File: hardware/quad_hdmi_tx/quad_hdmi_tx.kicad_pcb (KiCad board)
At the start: 4 copper layers, 115 x 110 mm, 147 parts, among them J1 HDMI_A, J2 HDMI_A, J3 HDMI_A, J4 HDMI_A, J5 USB-C 5V in, J6 5V ALT IN, J7 FPGA_J7, J8 FPGA_J8, U11 ADV7513BSWZ, U12 TPD12S016PWR, U13 TLV1117LV18DCYR, U21 ADV7513BSWZ, U22 TPD12S016PWR, U23 TLV1117LV18DCYR, U31 ADV7513BSWZ, U32 TPD12S016PWR, U33 TLV1117LV18DCYR, U41 ADV7513BSWZ, U42 TPD12S016PWR, U43 TLV1117LV18DCYR, U5 AP63203WU

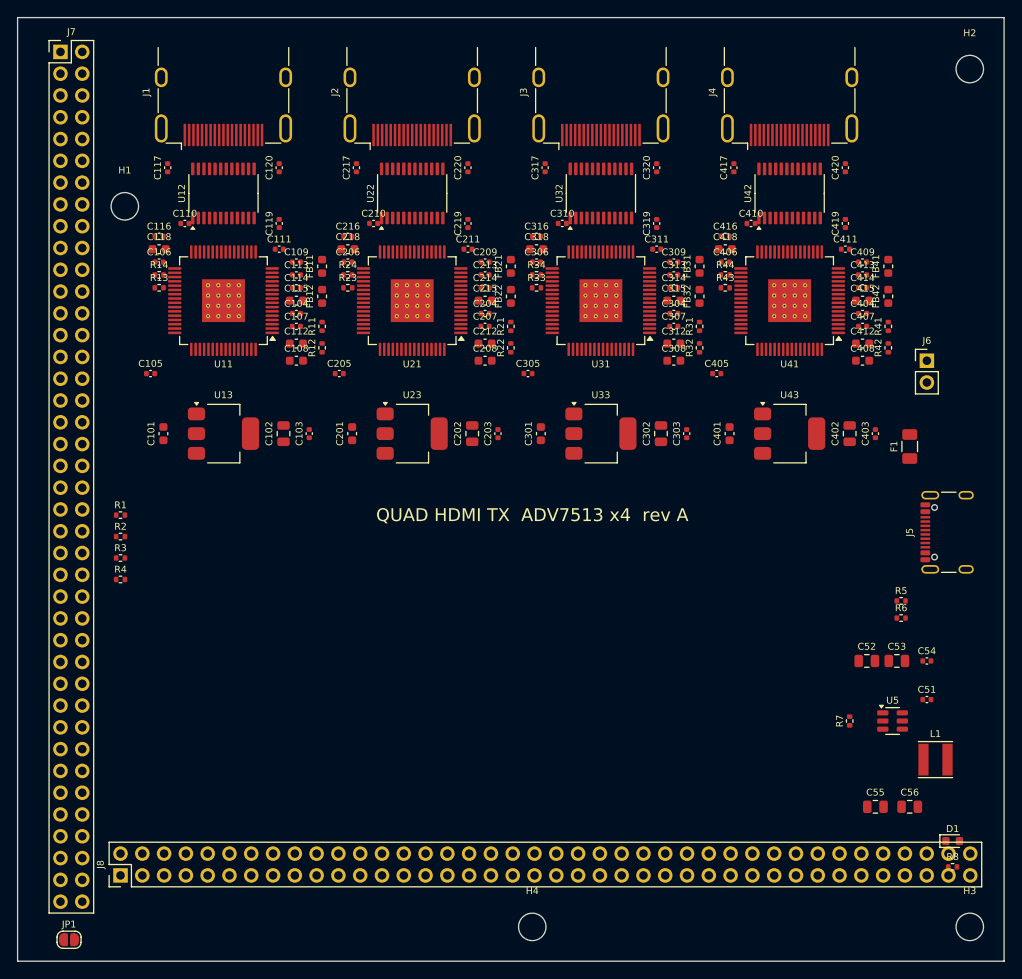
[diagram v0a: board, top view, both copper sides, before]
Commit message: レイアウト: プレーン系ネットのファンアウトビア生成、SES 取り込みの修正、チャネルピッチ 24 mm に変更
- FreeRouting は内層プレーンへのビアを作らないため、GND/+3V3/1V8 の全 SMD パッドに衝突チェック付きでビアを先置き
- 自前の SES パーサ (ses_import.py) を用意し、pcbnew API の取り込みが失敗した場合に使用
- FreeRouting の設定ファイル/GUI 要件などの注意点を README に記載

Co-Authored-By: Claude Fable 5.1 <noreply@anthropic.com>
Claude-Session: https://claude.ai/code/session_01JGo25NCpKCcdkj7JC5mDdQ
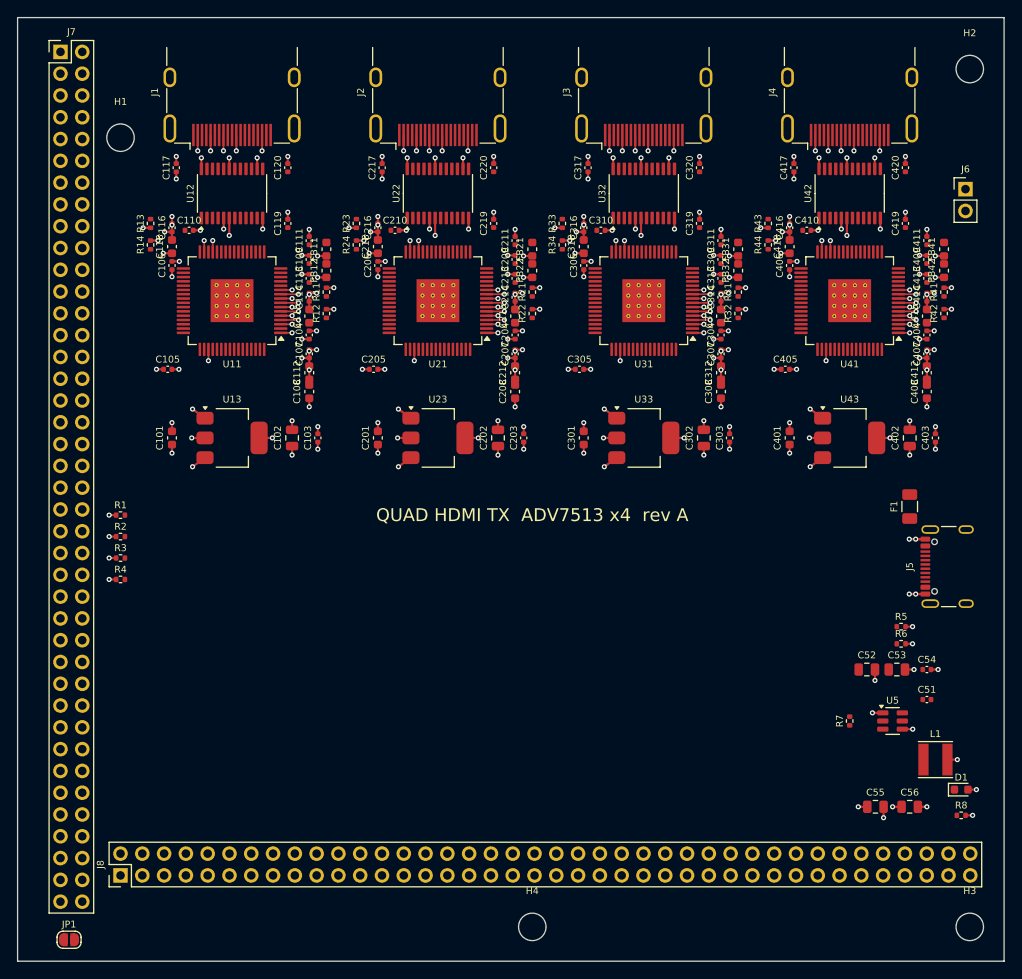
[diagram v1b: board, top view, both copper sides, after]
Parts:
- moved J6 20.5 mm to (110.5, 20.0)
- moved C411 9.55 mm to (106.0, 26.0), turned to 90 degrees
- moved R43 9.01 mm to (87.5, 24.0), turned to 90 degrees
- moved C408 8.32 mm to (106.0, 43.6), turned to 90 degrees
- moved C412 8.23 mm to (106.0, 41.4), turned to 90 degrees
- moved C407 8.15 mm to (106.0, 39.2), turned to 90 degrees
- moved R33 8.08 mm to (63.5, 24.0), turned to 90 degrees
- moved C405 8.02 mm to (89.5, 41.0)
- moved H1 8.02 mm to (12.0, 14.0)
- moved C404 7.91 mm to (106.0, 37.0), turned to 90 degrees
- moved C415 7.71 mm to (106.0, 34.8), turned to 90 degrees
- moved R41 7.63 mm to (108.0, 32.0)
- moved R42 7.63 mm to (108.0, 34.5)
- moved C414 7.58 mm to (106.0, 32.6), turned to 90 degrees
- moved C311 7.57 mm to (82.0, 26.0), turned to 90 degrees
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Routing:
- net GND: track 0.00 -> 224.3 mm, vias 0 -> 171
- net +3V3: track 0.00 -> 56.8 mm, vias 0 -> 51
- net CH4_1V8: track 0.00 -> 16.7 mm, vias 0 -> 15
- net CH1_1V8: track 0.00 -> 16.7 mm, vias 0 -> 15
- net CH3_1V8: track 0.00 -> 16.7 mm, vias 0 -> 15
- net CH2_1V8: track 0.00 -> 16.7 mm, vias 0 -> 15

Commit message: レイアウト: TMDS ペアを事前配線、ファンアウトの衝突チェック強化、配置とルールの修正
- TMDS 8 本/ch を ADV → TPD 下の U ターン → TPD パッド → コネクタ へ交差なしで固定配線
- ファンアウトビアは既存配線とも衝突チェック、内向き候補を追加、置けない GND ピンは隣接ピンへ短絡
- 1V8 の島を LDO 入力側と TPD 3.3V ビアを避ける多角形に変更、DVDD_3V ピン用スロット
- 最小ドリル 0.2 mm (ADV の EP サーマルビア)、コンデンサ列の間隔調整、シルクの参照記号を Fab 層へ
- 事前配線状態の DRC: クリアランス/コートヤード違反なし

Co-Authored-By: Claude Fable 5.1 <noreply@anthropic.com>
Claude-Session: https://claude.ai/code/session_01JGo25NCpKCcdkj7JC5mDdQ
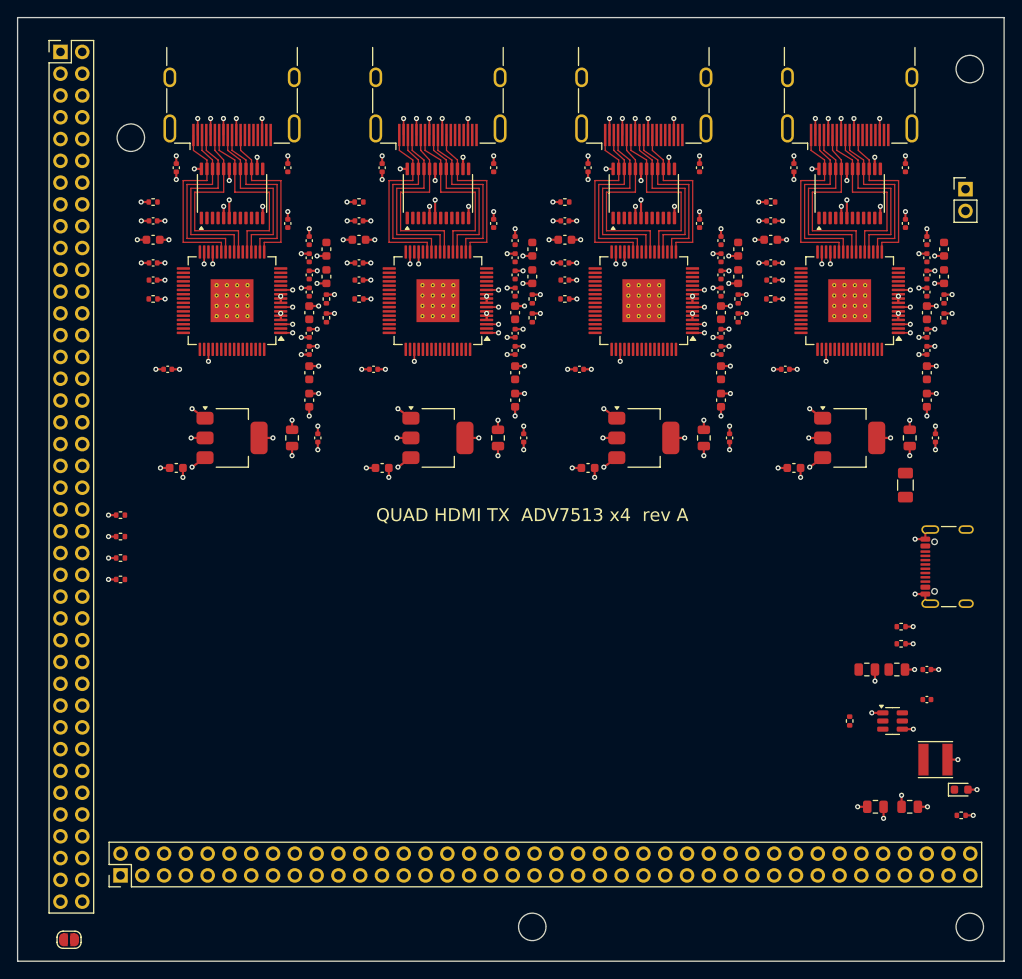
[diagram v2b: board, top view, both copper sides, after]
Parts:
- moved C210 7.16 mm to (39.8, 30.6)
- moved C310 7.16 mm to (63.8, 30.6)
- moved C410 7.16 mm to (87.8, 30.6)
- moved C110 7.16 mm to (15.8, 30.6)
- moved R14 6.31 mm to (15.8, 32.8), turned to 0 degrees
- moved R24 6.31 mm to (39.8, 32.8), turned to 0 degrees
- moved R34 6.31 mm to (63.8, 32.8), turned to 0 degrees
- moved R44 6.31 mm to (87.8, 32.8), turned to 0 degrees
- moved C101 3.54 mm to (18.5, 52.5), turned to 0 degrees
- moved C201 3.54 mm to (42.5, 52.5), turned to 0 degrees
- moved C301 3.54 mm to (66.5, 52.5), turned to 0 degrees
- moved C401 3.54 mm to (90.5, 52.5), turned to 0 degrees
- moved F1 2.55 mm to (103.5, 54.5)
- moved R13 2.52 mm to (15.8, 21.5), turned to 0 degrees
- moved R23 2.52 mm to (39.8, 21.5), turned to 0 degrees
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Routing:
- net GND: track 224.3 -> 191.0 mm, vias 171 -> 155
- net CH1_TX1_P: track 0.00 -> 22.5 mm
- net CH4_TX1_P: track 0.00 -> 22.5 mm
- net CH2_TX1_P: track 0.00 -> 22.5 mm
- net CH3_TX1_P: track 0.00 -> 22.5 mm
- net CH2_TX1_N: track 0.00 -> 22.5 mm
- net CH1_TX1_N: track 0.00 -> 22.5 mm
- net CH4_TX1_N: track 0.00 -> 22.5 mm
- net CH3_TX1_N: track 0.00 -> 22.5 mm
- net CH4_TX2_P: track 0.00 -> 21.7 mm
- net CH3_TX2_P: track 0.00 -> 21.7 mm
- net CH2_TX2_P: track 0.00 -> 21.7 mm
- net CH1_TX2_P: track 0.00 -> 21.7 mm
- net CH2_TX2_N: track 0.00 -> 21.7 mm
- net CH1_TX2_N: track 0.00 -> 21.7 mm
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
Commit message: レイアウト: 囲われたパッドへのアクセスビア、連続 GND ピンの数珠つなぎ、5V_OUT 事前配線、事前配線 DRC クリーン
Co-Authored-By: Claude Fable 5.1 <noreply@anthropic.com>
Claude-Session: https://claude.ai/code/session_01JGo25NCpKCcdkj7JC5mDdQ
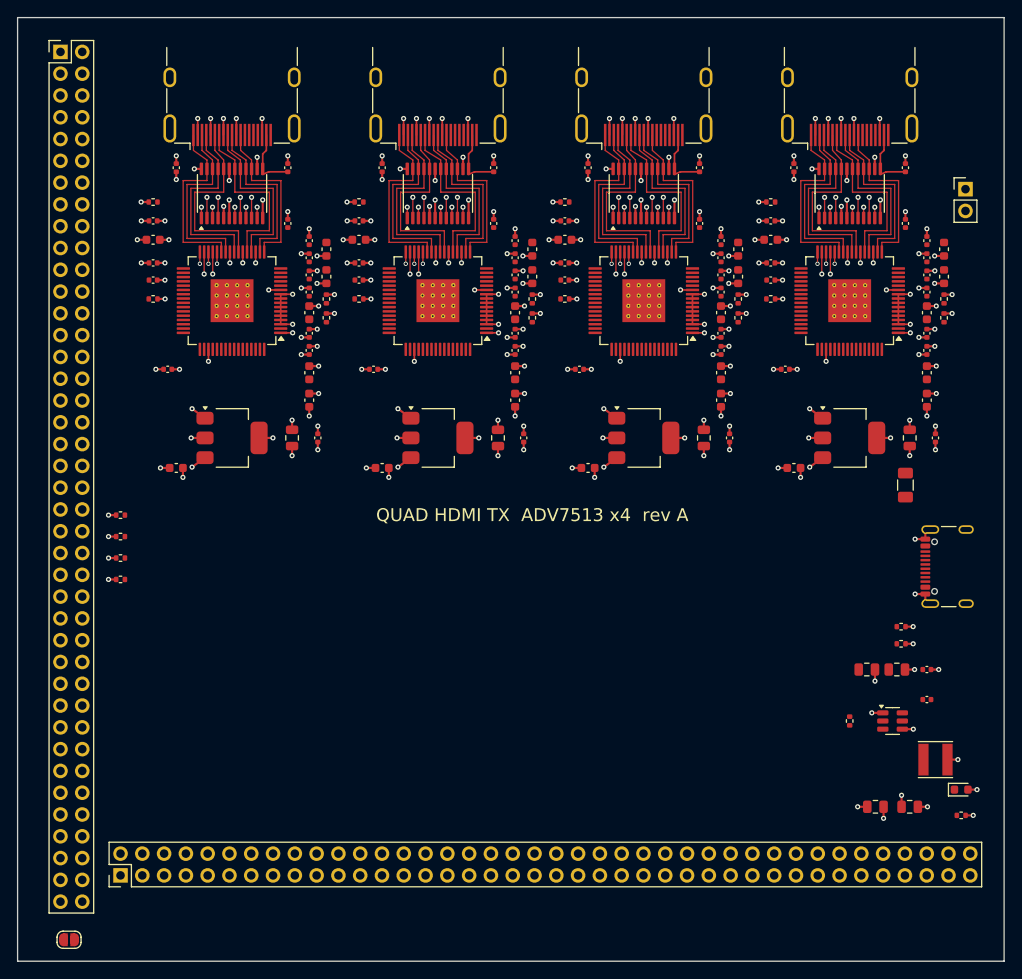
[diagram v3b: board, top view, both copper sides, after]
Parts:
- removed H1, H2, H3, H4: M3, MountingHole_3.2mm_M3
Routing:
- net +3V3: track 58.0 -> 65.7 mm
- net CH1_5V_OUT: track 0.00 -> 7.12 mm
- net CH4_5V_OUT: track 0.00 -> 7.12 mm
- net CH3_5V_OUT: track 0.00 -> 7.12 mm
- net CH2_5V_OUT: track 0.00 -> 7.12 mm
- net +5V: track 0.00 -> 5.05 mm, vias 0 -> 4
- net CH4_CEC_A: track 0.00 -> 2.64 mm, vias 0 -> 2
- net CH3_CEC_A: track 0.00 -> 2.64 mm, vias 0 -> 2
- net CH2_CEC_A: track 0.00 -> 2.64 mm, vias 0 -> 2
- net CH1_CEC_A: track 0.00 -> 2.64 mm, vias 0 -> 2
- net CH4_AVDD: track 0.00 -> 2.55 mm, vias 0 -> 2
- net CH3_AVDD: track 0.00 -> 2.55 mm, vias 0 -> 2
- net CH2_AVDD: track 0.00 -> 2.55 mm, vias 0 -> 2
- net CH1_AVDD: track 0.00 -> 2.55 mm, vias 0 -> 2
- net CH4_HPD_CONN: track 0.00 -> 2.41 mm, vias 0 -> 1
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
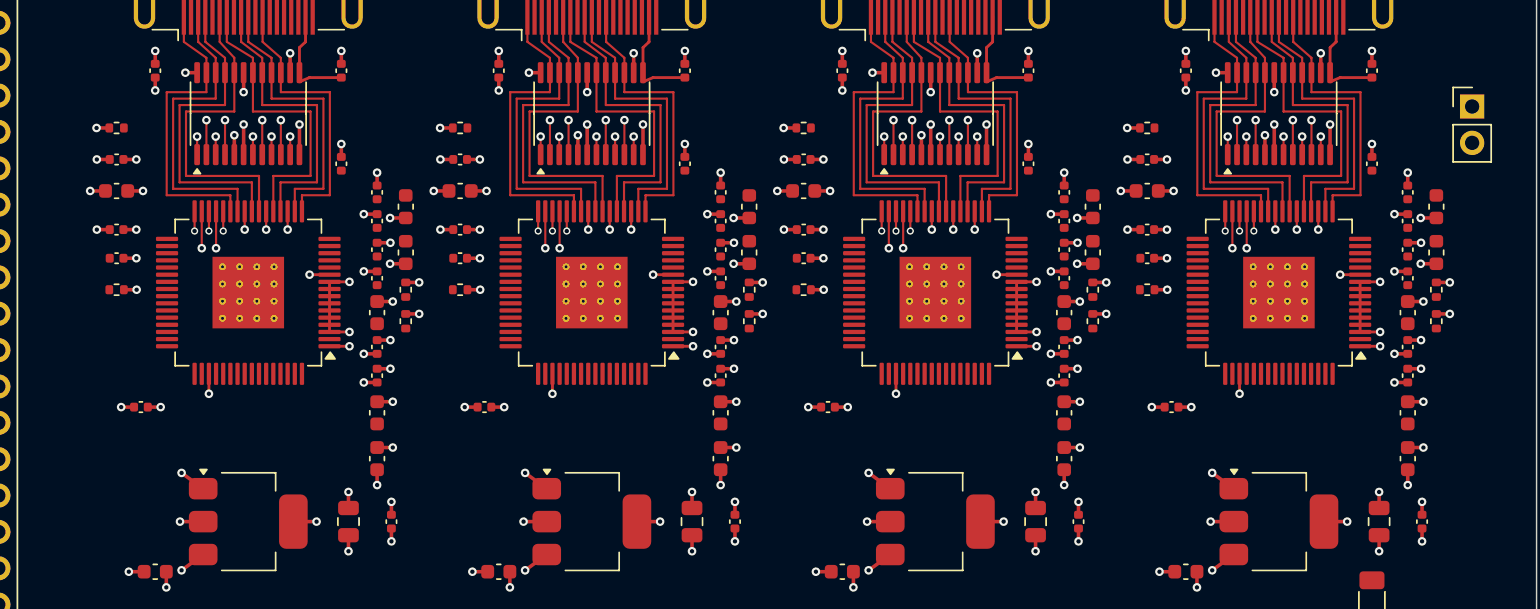
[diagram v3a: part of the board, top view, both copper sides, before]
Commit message: レイアウト: 左列を ADV 左上へ移動、1V8 の島を縮小、TPD 制御ピンと DVDD_3V の +3V3 事前配線、ビア掃除の修正
Co-Authored-By: Claude Fable 5.1 <noreply@anthropic.com>
Claude-Session: https://claude.ai/code/session_01JGo25NCpKCcdkj7JC5mDdQ
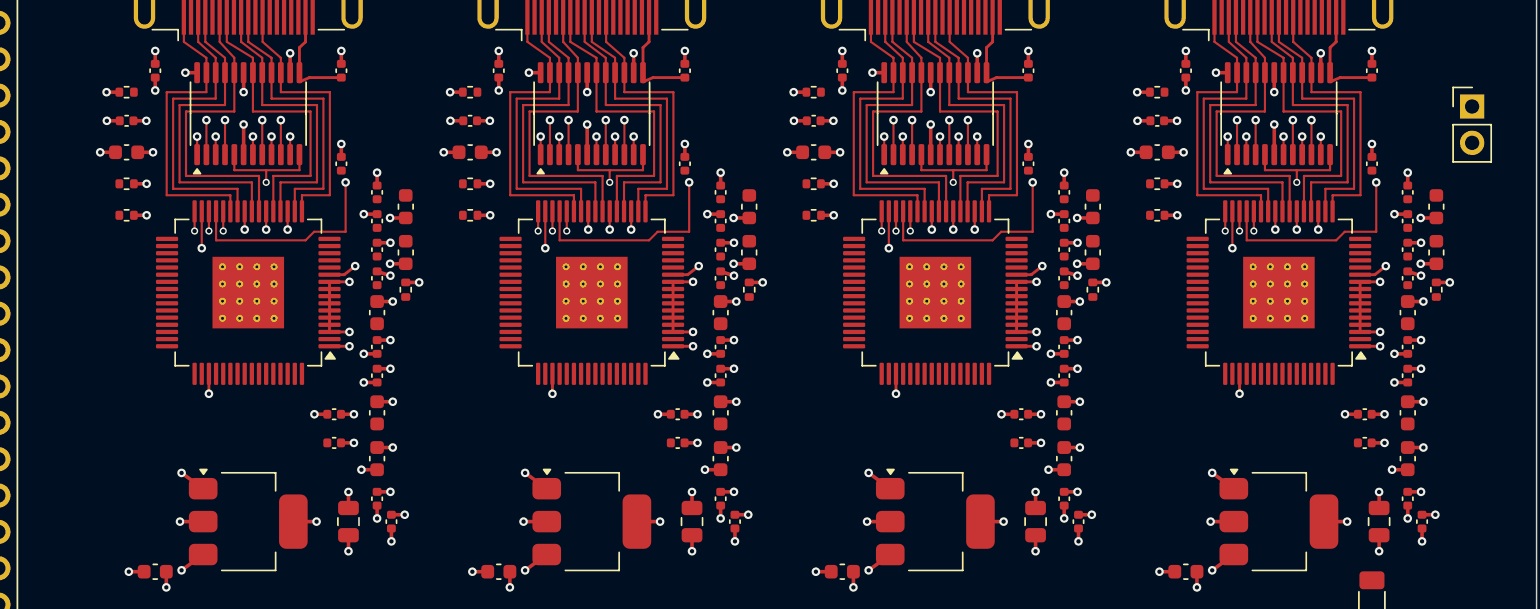
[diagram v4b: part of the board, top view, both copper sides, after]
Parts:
- moved C206 26.2 mm to (58.0, 47.4), turned to 90 degrees
- moved C306 26.2 mm to (82.0, 47.4), turned to 90 degrees
- moved C406 26.2 mm to (106.0, 47.4), turned to 90 degrees
- moved C106 26.2 mm to (34.0, 47.4), turned to 90 degrees
- moved R12 20.9 mm to (16.5, 27.6), turned to 0 degrees
- moved R22 20.9 mm to (40.5, 27.6), turned to 0 degrees
- moved R32 20.9 mm to (64.5, 27.6), turned to 0 degrees
- moved R42 20.9 mm to (88.5, 27.6), turned to 0 degrees
- moved C210 19.9 mm to (55.0, 43.5)
- moved C310 19.9 mm to (79.0, 43.5)
- moved C410 19.9 mm to (103.0, 43.5)
- moved C110 19.9 mm to (31.0, 43.5)
- moved C105 13.5 mm to (31.0, 41.5)
- moved C205 13.5 mm to (55.0, 41.5)
- moved C305 13.5 mm to (79.0, 41.5)
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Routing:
- net +3V3: track 65.7 -> 130.8 mm, vias 51 -> 47
- net CH3_1V8: track 18.9 -> 19.6 mm
- net CH1_1V8: track 18.9 -> 19.6 mm
- net CH4_1V8: track 18.9 -> 19.6 mm
- net CH2_1V8: track 18.9 -> 19.6 mm
